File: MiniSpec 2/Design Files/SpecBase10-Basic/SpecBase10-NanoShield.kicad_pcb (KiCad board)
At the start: 2 copper layers, 65 x 95 mm, 16 parts, among them J1 M20-8770642R, J2 M20-8770642R, J3 TSM-104-01-T-DH-P-TR

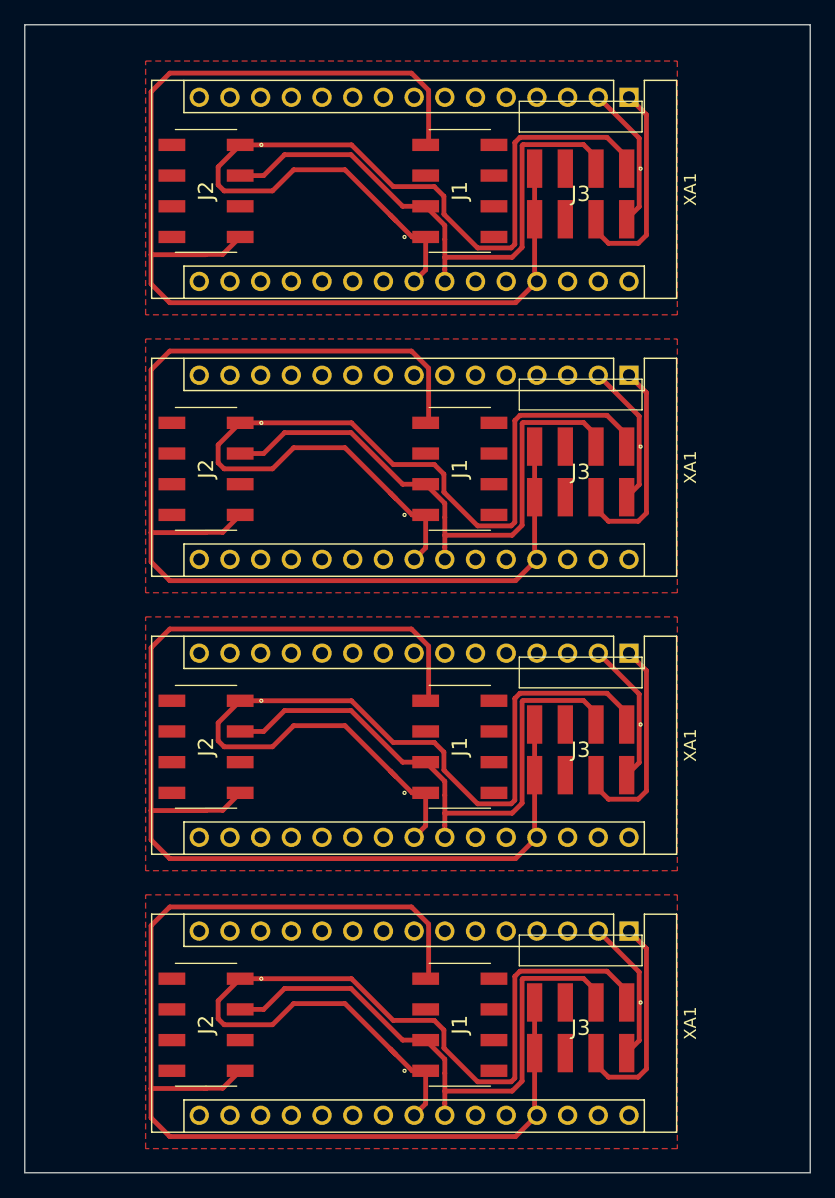
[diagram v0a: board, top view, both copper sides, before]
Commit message: big updates for 2 layer design with vias
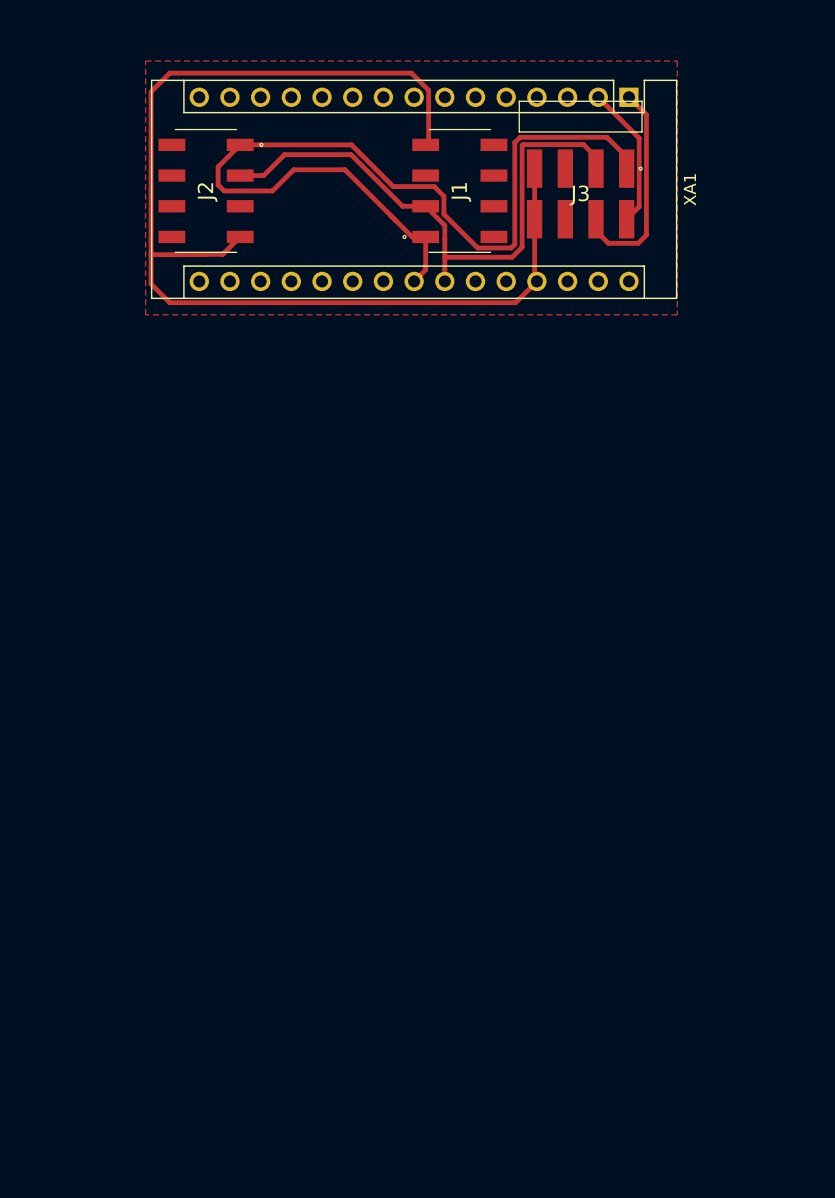
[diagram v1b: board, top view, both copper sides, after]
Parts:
- removed the J1 at (156.0, 132.8)
- removed the J1 at (156.0, 109.8)
- removed the J1 at (156.0, 86.8)
- removed the J2 at (135.0, 132.8)
- removed the J2 at (135.0, 109.8)
- removed the J2 at (135.0, 86.8)
- removed the J3 at (166.0, 133.0)
- removed the J3 at (166.0, 110.0)
- removed the J3 at (166.0, 87.0)
- removed the XA1 at (170.0, 125.0)
- removed the XA1 at (170.0, 102.0)
- removed the XA1 at (170.0, 79.0)
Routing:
- net +5V: track 382.1 -> 95.5 mm
- net SDA: track 303.8 -> 76.0 mm
- net SCL: track 189.6 -> 47.4 mm
- net BTN1: track 71.4 -> 17.8 mm
- net BTN2: track 47.7 -> 11.9 mm
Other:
- board outline removed
